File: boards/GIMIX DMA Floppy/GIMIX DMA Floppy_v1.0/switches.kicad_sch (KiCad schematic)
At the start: 15 parts, among them SW1 SW_DIP_x10, SW2 SW_DIP_x10, U36 74F04, U39 74LS32, U40 74LS136, U41 74LS136, U42 74LS136, U43 74LS136, U44 74LS136

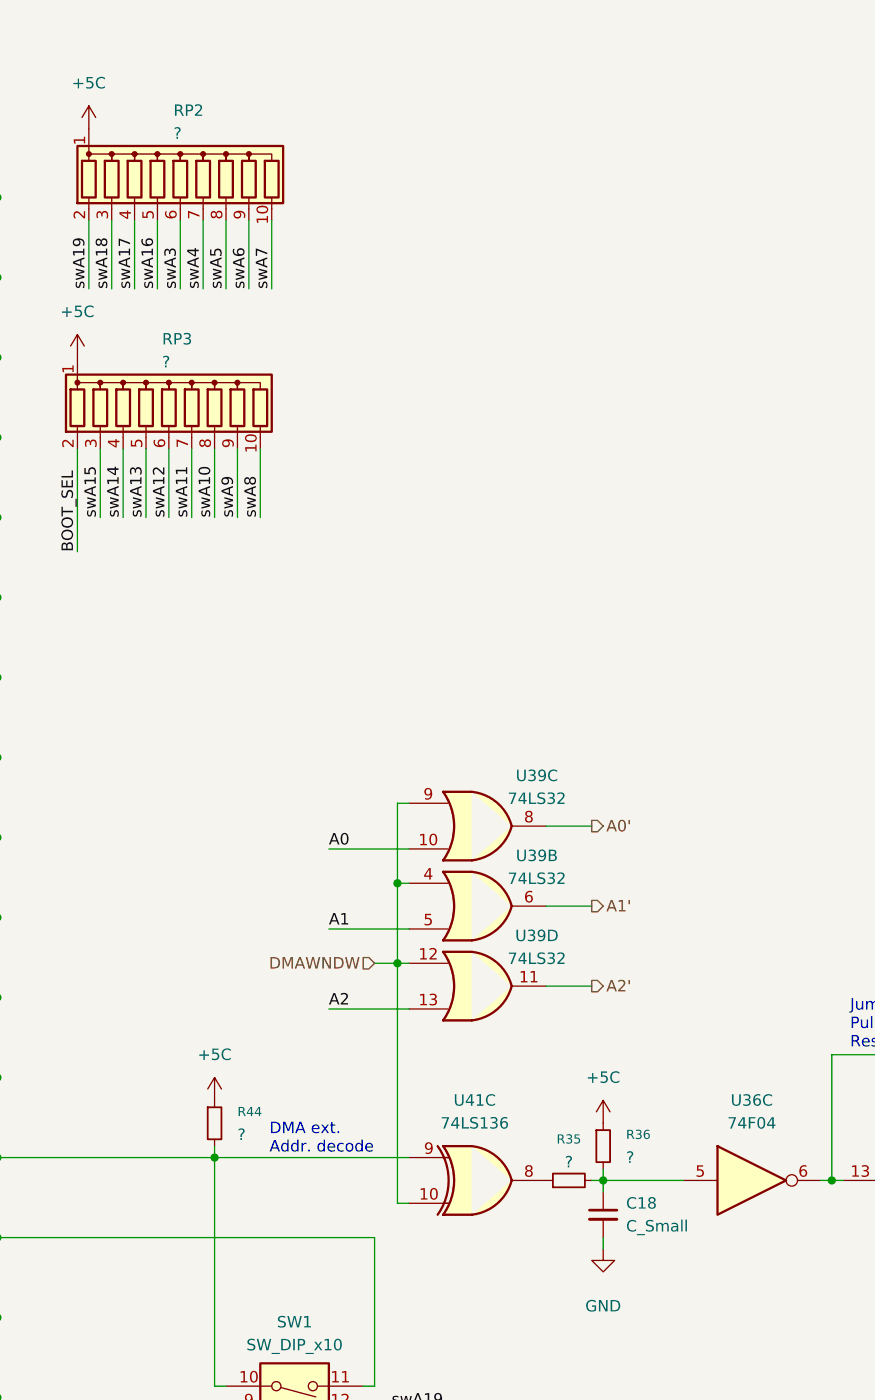
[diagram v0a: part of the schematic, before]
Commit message: DMA Floppy silkscreen and gerbers added
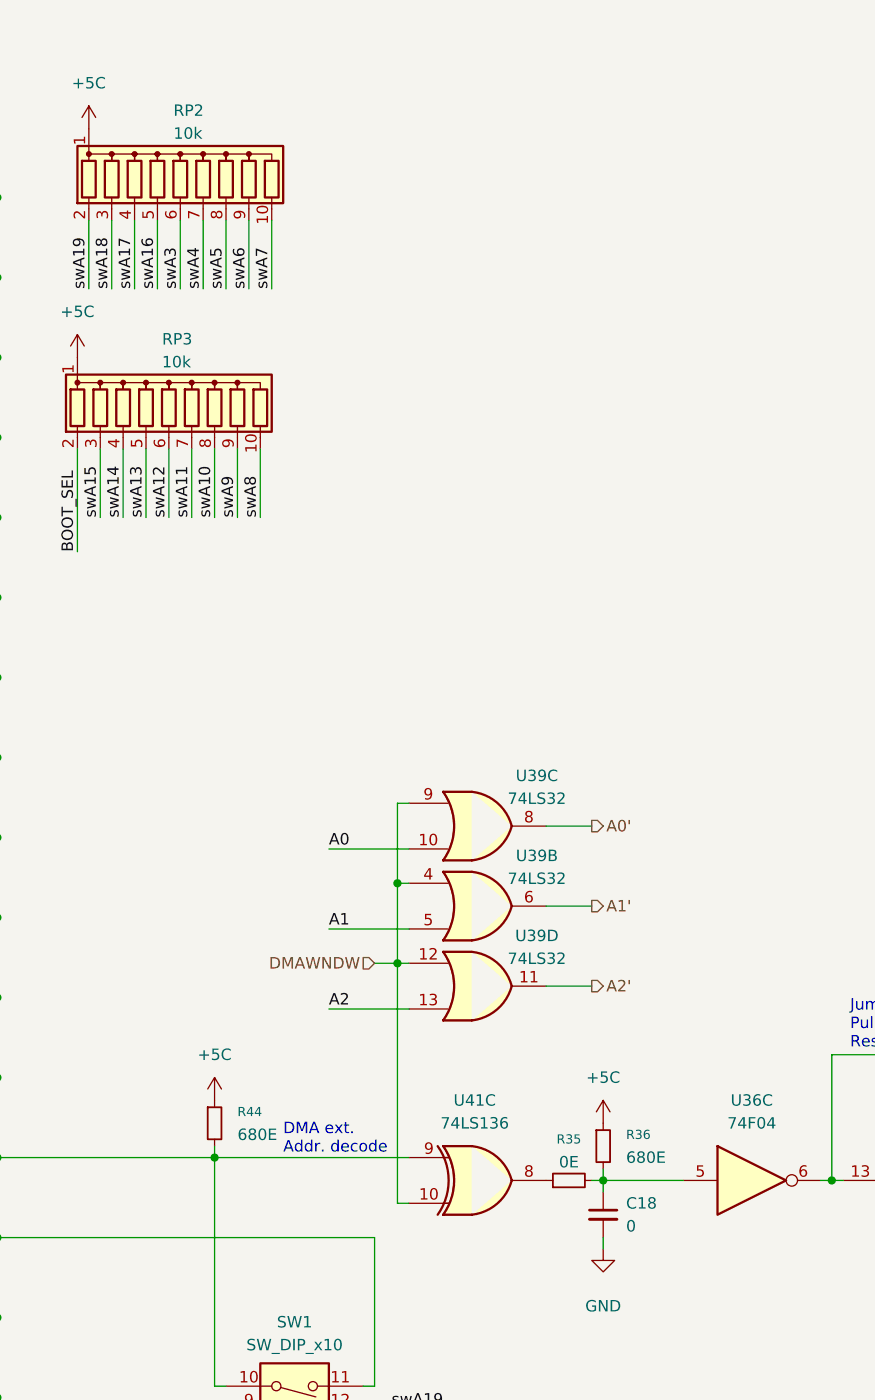
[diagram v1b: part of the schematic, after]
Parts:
- C18: value C_Small -> 0
- R35: value ? -> 0E
- R36, R44: value ? -> 680E
- RP2, RP3: value ? -> 10k
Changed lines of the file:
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@@
 	(text "DMA ext.\nAddr. decode"
 		(exclude_from_sim no)
-		(at 107.696 137.668 0)
+		(at 109.22 137.668 0)
 		(effects
 			(font
@@
 			)
 		)
-		(property "Value" "?"
+		(property "Value" "10k"
 			(at 95.758 51.308 0)
 			(effects
@@
 			)
 		)
-		(property "Value" "?"
+		(property "Value" "0E"
 			(at 140.97 140.208 90)
 			(effects
@@
 			)
 		)
-		(property "Value" "?"
+		(property "Value" "680E"
 			(at 147.32 139.6999 0)
 			(effects
@@
 			)
 		)
-		(property "Value" "C_Small"
+		(property "Value" "0"
 			(at 147.32 147.3262 0)
 			(effects
@@
 			)
 		)
-		(property "Value" "?"
+		(property "Value" "10k"
 			(at 97.028 25.908 0)
 			(effects
@@
 			)
 		)
-		(property "Value" "?"
+		(property "Value" "680E"
 			(at 104.14 137.1599 0)
 			(effects
